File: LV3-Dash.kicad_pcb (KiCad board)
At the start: 2 copper layers, 90 x 50 mm, 93 parts, among them J1 USB_C_Receptacle_USB2.0_16P, J2 FTSH-105-01-L-DV-K-A, J3 Conn_01x04_MountingPin, J4 Conn_01x05_Pin, J5 Conn_01x05_MountingPin, J6 MSD-11-A, J7 62684-401100AHLF, U1 STM32H743VITx, U2 TJA1051T-3, U3 TLV74033PDBVR, U4 LMR51625YDDCR, U5 TLV74033PDBVR, U6 AP3032KTR, Y1 Crystal_GND24

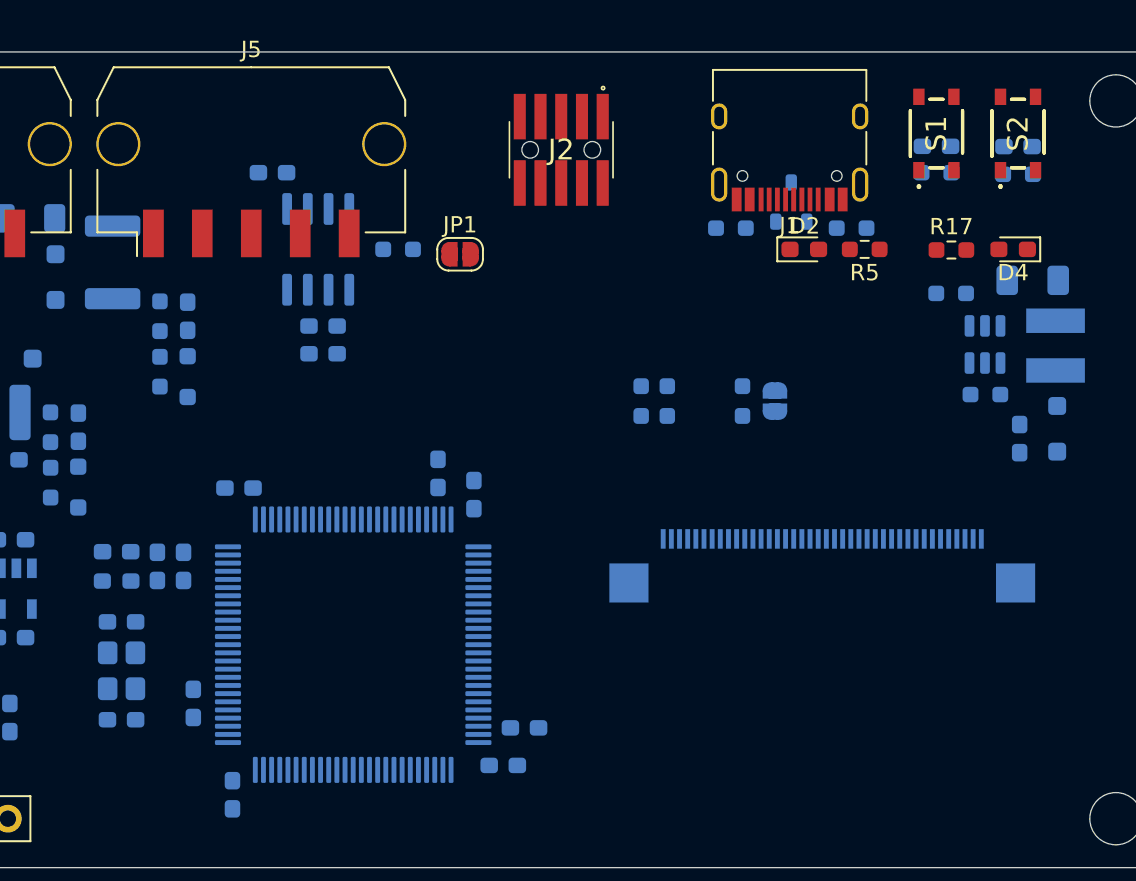
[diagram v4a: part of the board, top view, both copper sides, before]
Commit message: some preliminary routing
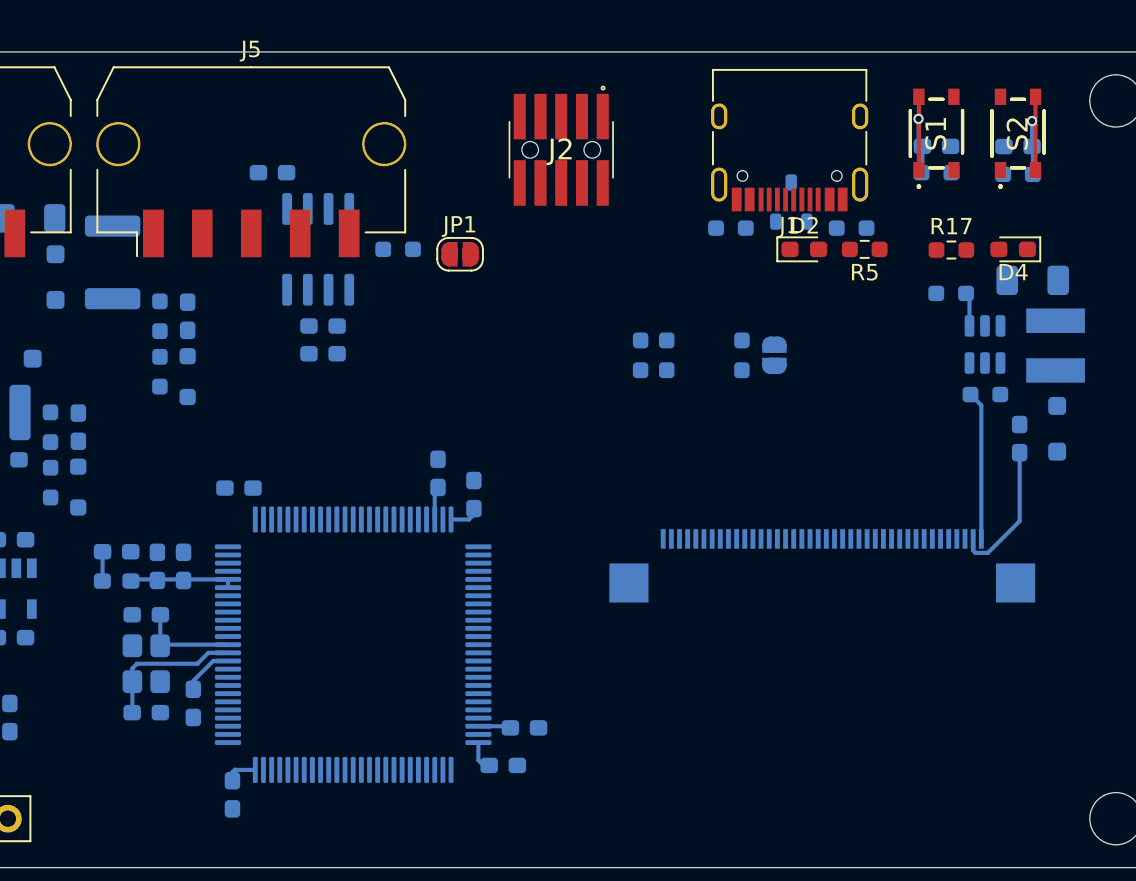
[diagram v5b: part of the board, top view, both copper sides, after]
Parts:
- moved R25 2.80 mm to (214.1, 88.6)
- moved R26 2.80 mm to (207.9, 88.6)
- moved R27 2.80 mm to (209.5, 88.6)
- moved JP2 2.80 mm to (216.1, 88.6)
- moved C10 1.58 mm to (177.6, 104.5)
- moved C9 1.58 mm to (177.6, 110.5)
- moved Y1 1.58 mm to (177.6, 107.5)
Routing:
- net +3.3V: track 0.00 -> 10.7 mm
- net BKLT-: track 0.00 -> 9.12 mm
- net HSE_IN: track 0.00 -> 8.97 mm
- net BKLT+: track 0.00 -> 8.62 mm
- net BOOT0: track 0.00 -> 7.96 mm, vias 0 -> 1
- net NRST: track 0.00 -> 7.94 mm, vias 0 -> 1
- net +VDDA: track 0.00 -> 6.49 mm
- net HSE_OUT: track 0.00 -> 6.09 mm
- net BKLT_CTRL: track 0.00 -> 2.08 mm
- net Net-(C13-Pad1): track 0.00 -> 2.05 mm
- net Net-(C14-Pad1): track 0.00 -> 2.00 mm

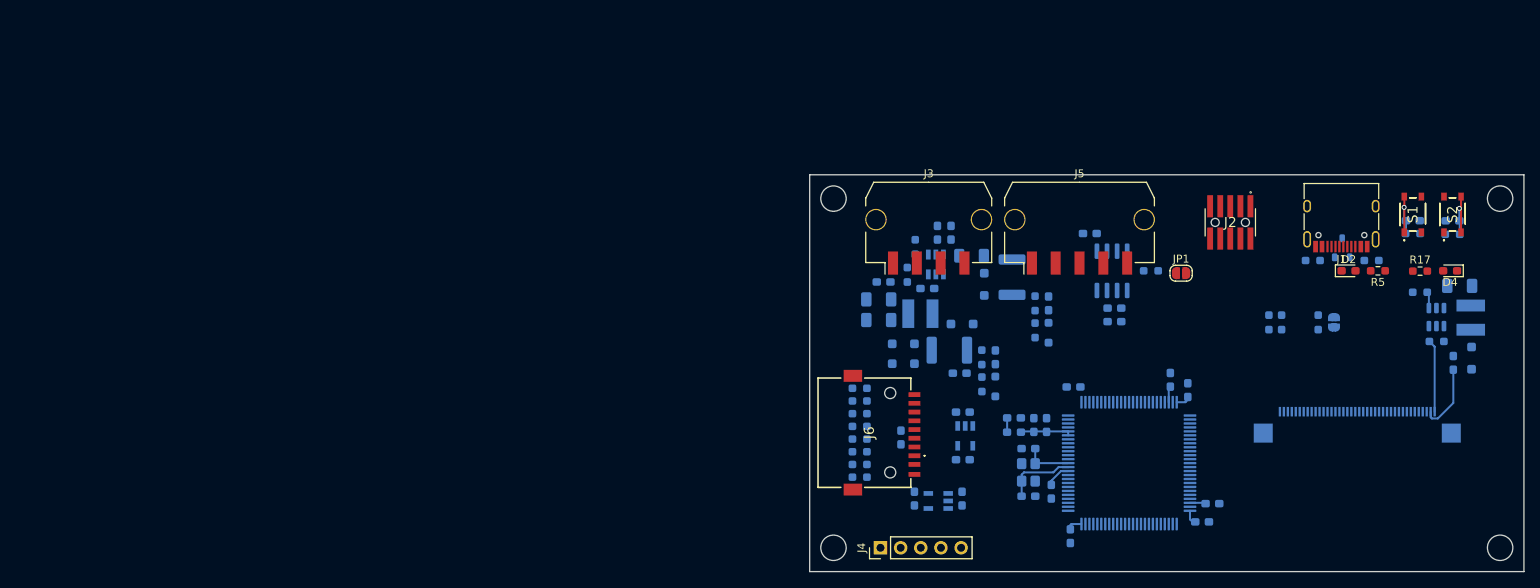
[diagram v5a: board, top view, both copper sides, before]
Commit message: finalize connector placement, modify layout
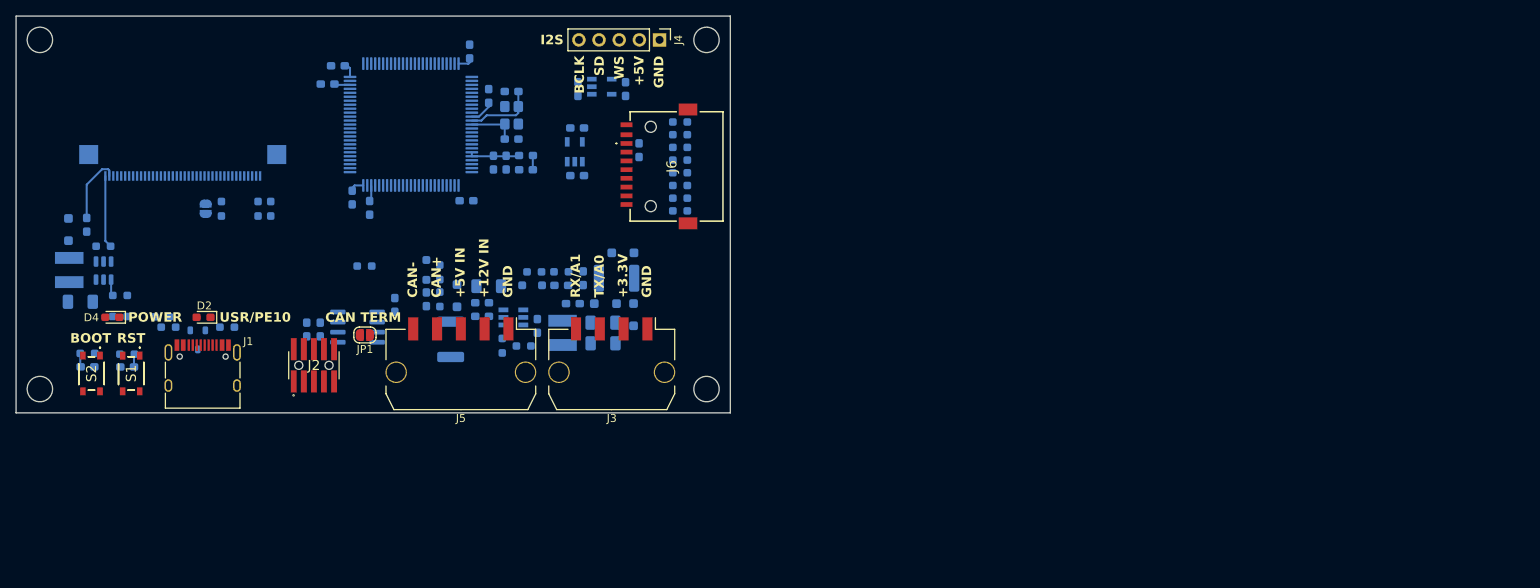
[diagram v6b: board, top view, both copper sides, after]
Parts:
- R17, R5: moved to B.Cu
- moved D10 177.5 mm to (56.6, 76.9), turned to -90 degrees
- moved L3 176.7 mm to (56.7, 82.0), turned to 90 degrees
- moved C32 173.8 mm to (58.1, 86.0), turned to 180 degrees
- moved C33 173.1 mm to (58.9, 76.3), turned to -90 degrees
- moved C12 173.0 mm to (59.0, 94.2), turned to 0 degrees
- moved S2 172.7 mm to (59.5, 95.0), turned to -90 degrees
- moved R2 172.7 mm to (59.0, 92.5), turned to 180 degrees
- moved D4 168.7 mm to (62.1, 88.0)
- moved R24 168.4 mm to (61.0, 79.0), turned to 180 degrees
- moved U6 168.1 mm to (61.0, 82.1), turned to -90 degrees
- moved R17 163.9 mm to (63.1, 87.9)
- moved R23 163.8 mm to (63.1, 85.2), turned to 180 degrees
- moved C11 163.1 mm to (64.0, 94.2), turned to 180 degrees
- moved S1 162.7 mm to (64.5, 95.0), turned to -90 degrees
- moved R1 162.7 mm to (64.0, 92.6), turned to 180 degrees
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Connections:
- J4 pad 2: +3.3V_AUX -> +5V
- J7 pad 13: LCD_G6 -> unconnected-(J7-Pad13)
- J7 pad 14: LCD_G7 -> unconnected-(J7-Pad14)
- J7 pad 21: LCD_B6 -> unconnected-(J7-Pad21)
- J7 pad 22: LCD_B7 -> unconnected-(J7-Pad22)
- J7 pad 5: LCD_R6 -> unconnected-(J7-Pad5)
- J7 pad 6: LCD_R7 -> unconnected-(J7-Pad6)
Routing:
- net NRST: track 7.94 -> 1.64 mm, vias 1 -> 0
- net BOOT0: track 7.96 -> 1.72 mm, vias 1 -> 0
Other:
- board text added: "+12V IN"
- board text added: "+3.3V"
- board text added: "+5V"
- board text added: "+5V IN"
- board text added: "BCLK"
- board text added: "BOOT"
- board text added: "CAN TERM"
- board text added: "CAN+"
- board text added: "CAN-"
- board text added: "GND"
- board text added: "I2S"
- board text added: "POWER"
- board text added: "RST"
- board text added: "RX/A1"
- board text added: "SD"
- board text added: "TX/A0"
- board text added: "USR/PE10"
- board text added: "WS"

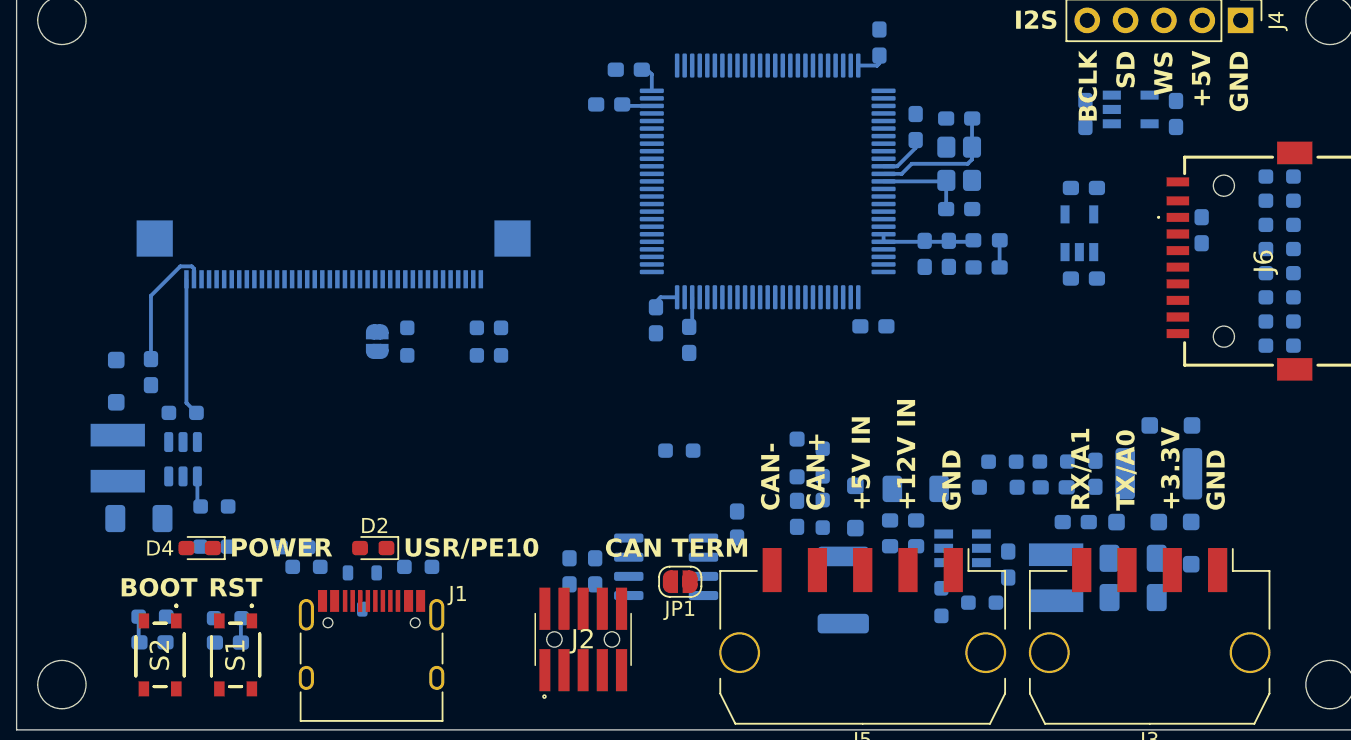
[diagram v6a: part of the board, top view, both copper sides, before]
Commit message: 3.3v regulator changes, GPIO output fixes, layout changes
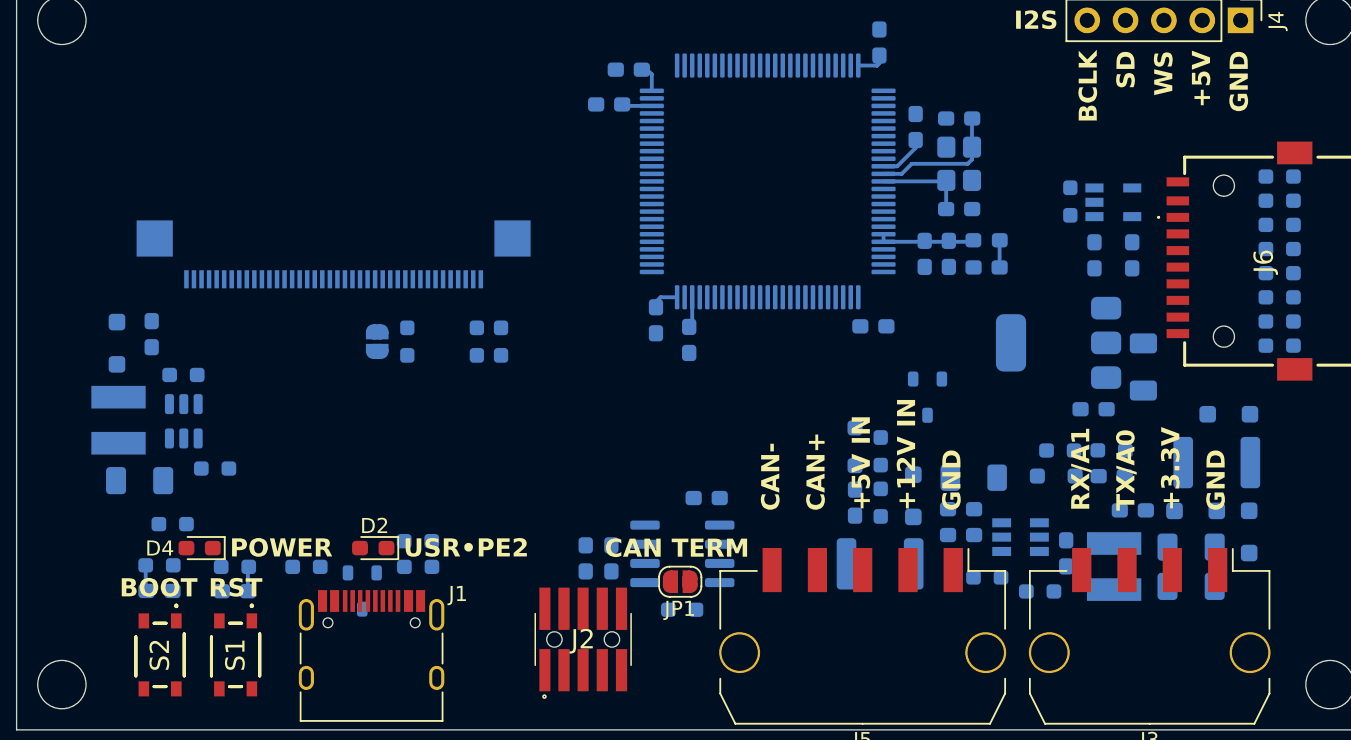
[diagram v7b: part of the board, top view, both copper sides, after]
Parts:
- removed C18, C19, C28: 1u, Capacitor_SMD:C_0603_1608Metric_Pad1.08x0.95mm_HandSolder
- removed U3: TLV74033PDBVR, SamacSys_Parts:SOT95P280X145-5N
- added C34: 1u, Capacitor_SMD:C_0603_1608Metric_Pad1.08x0.95mm_HandSolder, B.Cu at (121.4, 68.6)
- added D11: PESD2USB3UV, Package_TO_SOT_SMD:SOT-23W, B.Cu at (110.3, 78.0)
- added R28: 5.1k, Resistor_SMD:R_0603_1608Metric_Pad0.98x0.95mm_HandSolder, B.Cu at (119.8, 65.0)
- added U7: AMS1117-3.3, Package_TO_SOT_SMD:SOT-223-3_TabPin2, B.Cu at (119.0, 74.4)
- C20: value 100n -> 1u
- C31: value 1u -> 22u; footprint Capacitor_SMD:C_0603_1608Metric_Pad1.08x0.95mm_HandSolder -> Capacitor_SMD:C_1206_3216Metric_Pad1.33x1.80mm_HandSolder
- moved C31 12.5 mm to (124.6, 76.0), turned to -90 degrees
- moved R6 10.5 mm to (94.1, 92.0)
- moved C30 8.68 mm to (121.3, 78.8)
- moved R5 8.20 mm to (76.6, 87.5)
- moved C20 4.89 mm to (123.9, 68.6), turned to -90 degrees
- moved C23 3.91 mm to (127.8, 87.9)
- moved C27 3.91 mm to (112.6, 87.1)
- moved D7 3.91 mm to (130.3, 79.1)
- moved C22 3.91 mm to (119.5, 88.3)
- moved C24 3.91 mm to (127.8, 90.5)
- moved C26 3.91 mm to (112.6, 85.4)
- moved C29 3.91 mm to (122.5, 83.2)
- moved D8 3.91 mm to (118.9, 83.2)
- moved R18 3.91 mm to (117.8, 90.8)
- moved R22 3.91 mm to (119.1, 81.5)
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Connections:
- C20 pad 1: +3.3V -> +3.3V_SD
- J3 pad 2: +3.3V_AUX -> +3.3V
- J6 pad P4: +3.3V -> +3.3V_SD
- J7 pad 13: unconnected-(J7-Pad13) -> LCD_G6
- J7 pad 14: unconnected-(J7-Pad14) -> LCD_G7
- J7 pad 21: unconnected-(J7-Pad21) -> LCD_B6
- J7 pad 22: unconnected-(J7-Pad22) -> LCD_B7
- J7 pad 5: unconnected-(J7-Pad5) -> LCD_R6
- J7 pad 6: unconnected-(J7-Pad6) -> LCD_R7
- R10 pad 2: +3.3V -> +3.3V_SD
- R11 pad 2: +3.3V -> +3.3V_SD
- R12 pad 2: +3.3V -> +3.3V_SD
- R13 pad 2: +3.3V -> +3.3V_SD
- R14 pad 2: +3.3V -> +3.3V_SD
- R7 pad 2: +3.3V -> +3.3V_SD
- R8 pad 2: +3.3V -> +3.3V_SD
- R9 pad 2: +3.3V -> +3.3V_SD
- U1 pad 1: unconnected-(U1-PE2-Pad1) -> LED_USR
- U1 pad 2: unconnected-(U1-PE3-Pad2) -> SD_EN
- U5 pad 3: +5V -> SD_EN
- U5 pad 5: +3.3V -> +3.3V_SD
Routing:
- net BKLT-: track 9.12 -> 0.00 mm
- net BKLT+: track 8.62 -> 0.00 mm
- net BKLT_CTRL: track 2.08 -> 0.00 mm
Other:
- board text added: "USR•PE2"
- board text removed: "USR/PE10"
